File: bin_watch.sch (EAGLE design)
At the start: 69 parts, among them IC1 MEGA48/88/168-AU, Q1 8MHz, T1 NX3008NBKV, T2 NX3008NBKV, T3 NX3008NBKV, T4 NX3008NBKV, T5 PMDT670UPE, T6 PMDT670UPE, T7 PMDT670UPE

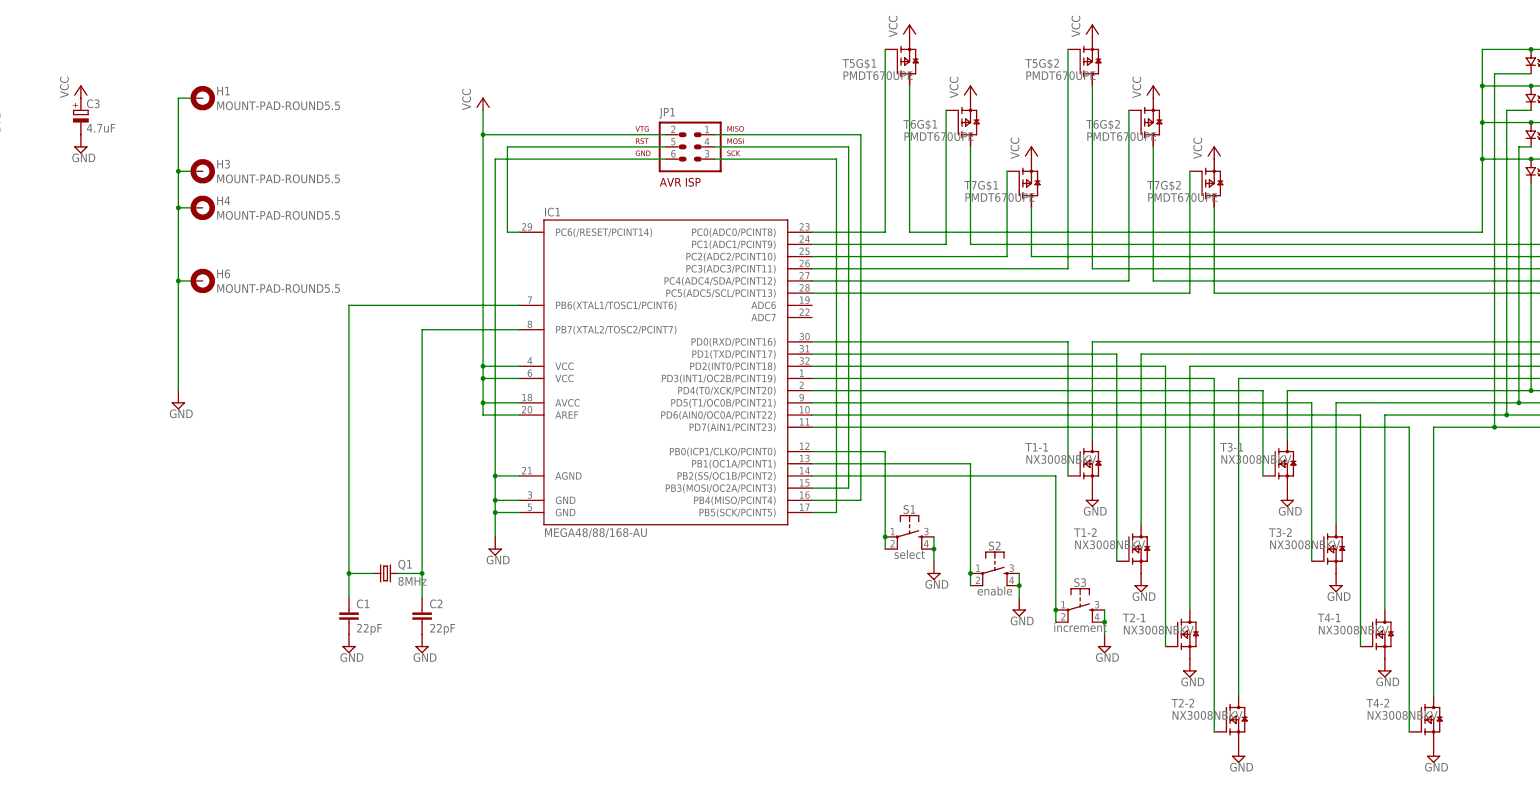
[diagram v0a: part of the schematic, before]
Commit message: Route cleanup
I ditched the auto-routed traces, and hand-routed everything. This should be much easier to work with.
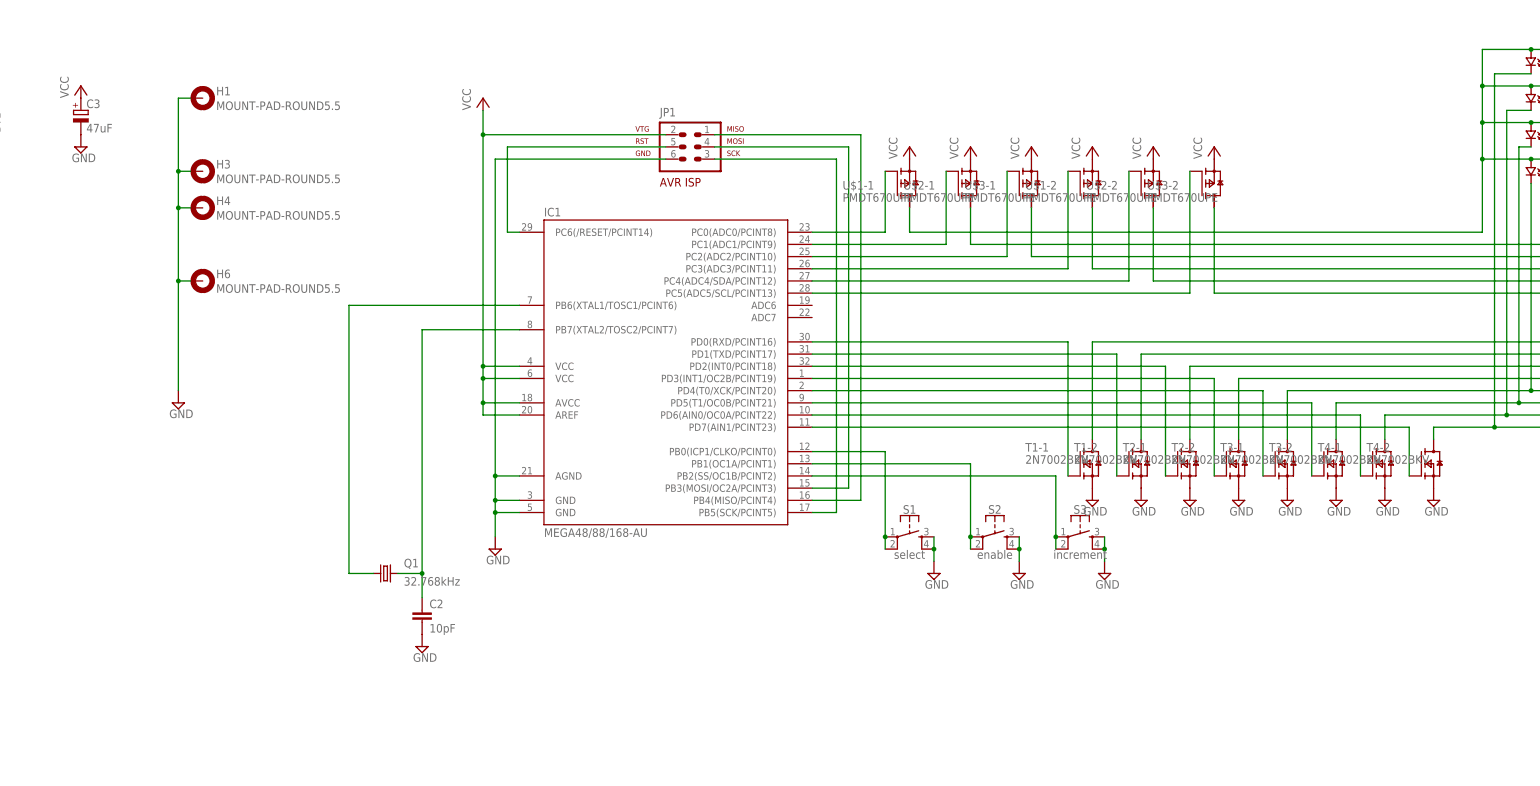
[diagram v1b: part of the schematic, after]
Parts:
- removed C1: 22pF, rcl:C-EUC0805
- removed T5, T6, T7: PMDT670UPE, nxp_60:PMDT670UPE
- added U$1, U$2, U$3: PMDT670UPE, nxp_60:PMDT670UPE
- C2: value 22pF -> 10pF
- C3: value 4.7uF -> 47uF
- Q1: value 8MHz -> 32.768kHz; device crystal:CRYSTALCTS406 -> crystal-geyer_V1_0:KX-327-NHF
- T1, T2, T3, T4: value NX3008NBKV -> 2N7002BKV
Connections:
- net XTAL2 renamed XTAL_N
- removed net XTAL1: C1.1, IC1.PB6(XTAL1/TOSC1/PCINT6), Q1.1
- new net XTAL_P: IC1.PB6(XTAL1/TOSC1/PCINT6), Q1.1
- net BLOCK: now also U$3-2.D; no longer T7G$2.D
- net BLOCK0: now also U$1-1.D; no longer T5G$1.D
- net BLOCK1: now also U$2-1.D; no longer T6G$1.D
- net BLOCK2: now also U$3-1.D; no longer T7G$1.D
- net BLOCK3: now also U$1-2.D; no longer T5G$2.D
- net BLOCK4: now also U$2-2.D; no longer T6G$2.D
- net GND: no longer C1.2
- net PC0: now also U$1-1.G; no longer T5G$1.G
- net PC1: now also U$2-1.G; no longer T6G$1.G
- net PC2: now also U$3-1.G; no longer T7G$1.G
- net PC3: now also U$1-2.G; no longer T5G$2.G
- net PC4: now also U$2-2.G; no longer T6G$2.G
- net PC5: now also U$3-2.G; no longer T7G$2.G
- net VCC: now also U$1-1.S, U$1-2.S, U$2-1.S, U$2-2.S, U$3-1.S, U$3-2.S; no longer T5G$1.S, T5G$2.S, T6G$1.S, T6G$2.S, T7G$1.S, T7G$2.S
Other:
- moved on the sheet: S2, S3, T1-2, T2-1, T2-2, T3-2, T4-1, T4-2

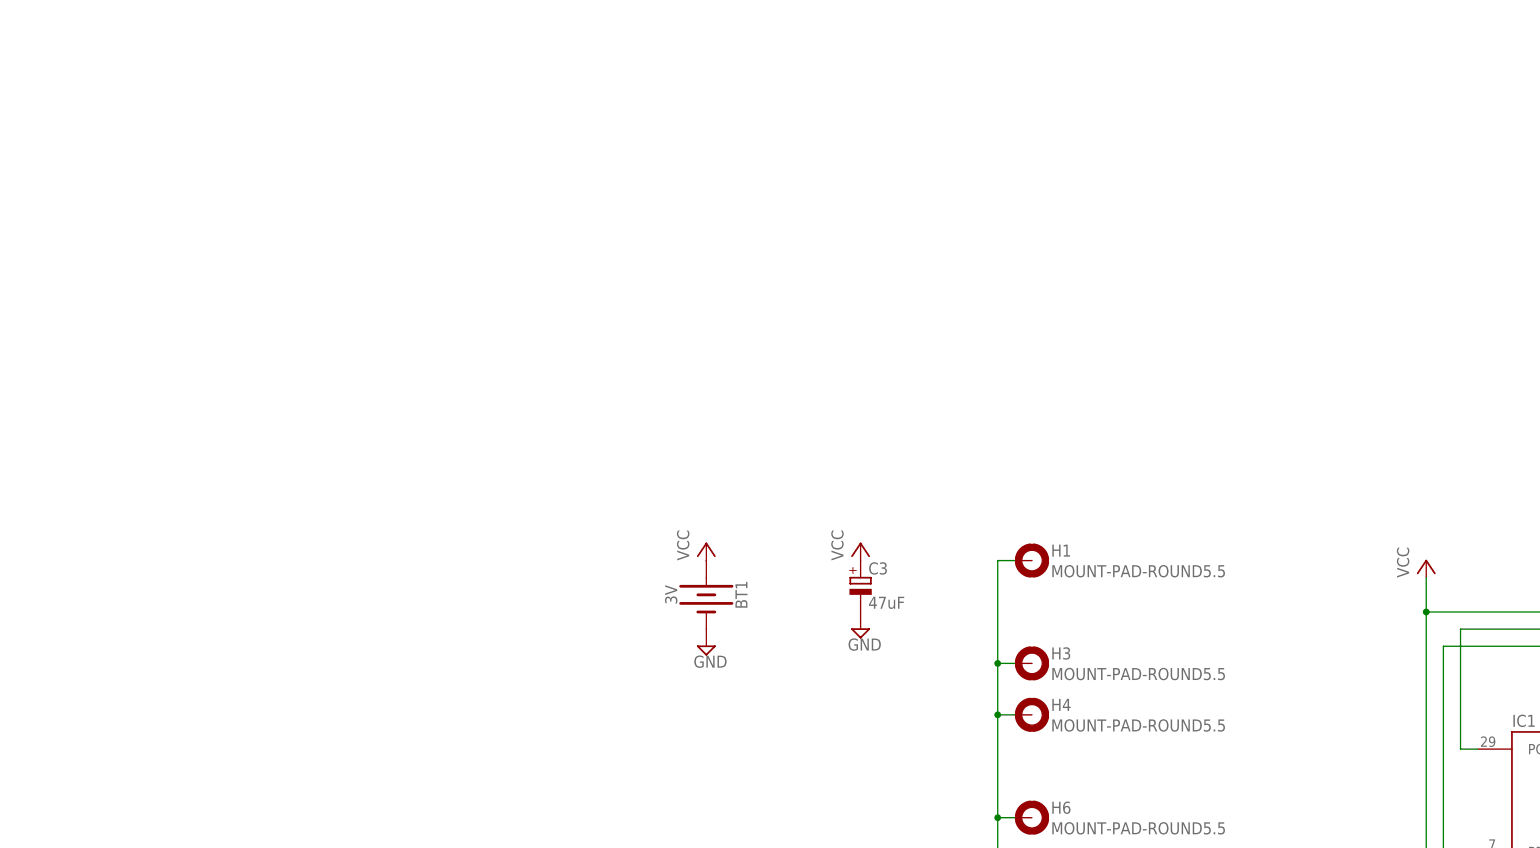
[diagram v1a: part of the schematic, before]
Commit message: Switched to Li-ion
The button cell i not up to the task, so we need a Li-ion battery.
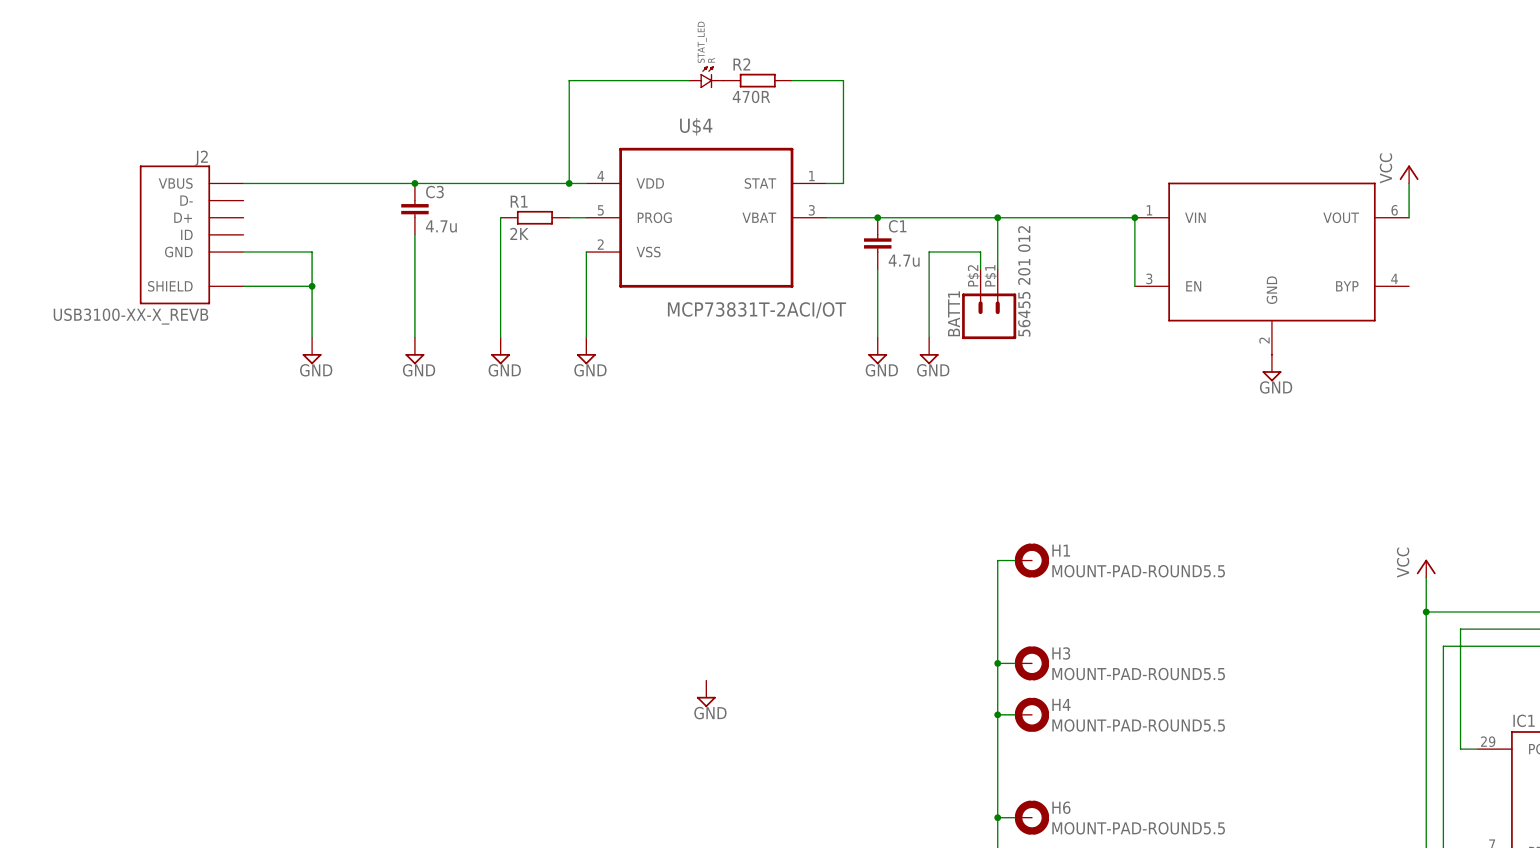
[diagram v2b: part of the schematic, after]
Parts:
- removed BT1: 3V, SparkFun-Batteries:BATTERY-12MM_SMD
- added BATT1: 56455 201 012, SparkFun-Connectors:CONN_02PTH2
- added C1: 4.7u, rcl:C-EUC0805
- added J2: USB3100-XX-X_REVB, USB3100-XX-X_REVB:USB3100-XX-X_REVB
- added R1: 2K, rcl:R-EU_R0805
- added R2: 470R, rcl:R-EU_R0805
- added STAT_LED: R, standardparts:LED.0603
- added U$4: MCP73831T-2ACI/OT, Microchip_By_element14_Batch_1:MCP73831T-2ACI/OT
- added U$5: MIC5319-3.3YD5-TR, pmg-library:MIC5319-3.3YD5-TR
- C3: value 47uF -> 4.7u; device rcl:CPOL-EU153CLV-0505 -> rcl:C-EUC0805
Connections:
- new net N$3: R2.1, STAT_LED.2
- new net PROG: R1.2, U$4.PROG
- new net STAT: R2.2, U$4.STAT
- new net VBATT: BATT1.1, C1.1, U$4.VBAT, U$5.EN, U$5.VIN
- new net VBUS: C3.1, J2.VBUS, STAT_LED.1, U$4.VDD
- net GND: now also BATT1.2, C1.2, C3.2, J2.GND, J2.SHIELD, R1.1, U$4.VSS, U$5.GND; no longer BT1.-, C3.-
- net VCC: now also U$5.VOUT; no longer BT1.+, C3.+

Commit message: Switched to switching supply
The linear regulator is not very efficient, swapping it for a buck converter.
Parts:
- removed J2: USB3100-XX-X_REVB, USB3100-XX-X_REVB:USB3100-XX-X_REVB
- removed U$2: PMDT670UPE, nxp_60:PMDT670UPE
- removed U$4: MCP73831T-2ACI/OT, Microchip_By_element14_Batch_1:MCP73831T-2ACI/OT
- removed U$5: MIC5319-3.3YD5-TR, pmg-library:MIC5319-3.3YD5-TR
- added C4: 3p, rcl:C-EUC0805
- added C5: (no value), rcl:CPOL-EUB/3528-21R
- added J1: USB3100-XX-X_REVB, USB3100-XX-X_REVB:USB3100-XX-X_REVB
- added L1: 2.2u, inductor:COIL-HI
- added R3: 294K, rcl:R-EU_R0805
- added R4: 470R, rcl:R-EU_R0805
- added T6: PMDT670UPE, nxp_60:PMDT670UPE
- added U1: MCP73831T-2ACI/OT, Microchip_By_element14_Batch_1:MCP73831T-2ACI/OT
- added U2: RT8059, pmg-library:RT8059
- C1: value 4.7u -> 10pF
- C2: value 10pF -> 4.7u
- R2: value 470R -> 1M33
- renumbered U$1 to T5, U$3 to T7
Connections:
- new net ADC6: IC1.ADC6
- new net ADC7: IC1.ADC7
- new net FB: C4.1, R2.1, R3.2, U2.FB
- new net LX: L1.L, U2.LX
- net BLOCK1: now also T6-1.D; no longer U$2-1.D
- net BLOCK4: now also T6-2.D; no longer U$2-2.D
- net GND: now also C5.-, J1.GND, J1.SHIELD, R3.1, U1.VSS, U2.GND; no longer J2.GND, J2.SHIELD, U$4.VSS, U$5.GND
- net N$3: now also R4.1; no longer R2.1
- net PC1: now also T6-1.G; no longer U$2-1.G
- net PC4: now also T6-2.G; no longer U$2-2.G
- net PROG: now also U1.PROG; no longer U$4.PROG
- net STAT: now also R4.2, U1.STAT; no longer R2.2, U$4.STAT
- net VBATT: now also C3.1, U1.VBAT, U2.EN, U2.VIN; no longer C1.1, U$4.VBAT, U$5.EN, U$5.VIN
- net VBUS: now also C2.1, J1.VBUS, U1.VDD; no longer C3.1, J2.VBUS, U$4.VDD
- net VCC: now also C4.2, C5.+, L1.R, R2.2, T6-1.S, T6-2.S; no longer U$2-1.S, U$2-2.S, U$5.VOUT
- net XTAL_N: now also C1.1; no longer C2.1
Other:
- moved on the sheet: BATT1, C1, C2, C3, H1, H3, H4, H6, R1, R2, S1, S2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

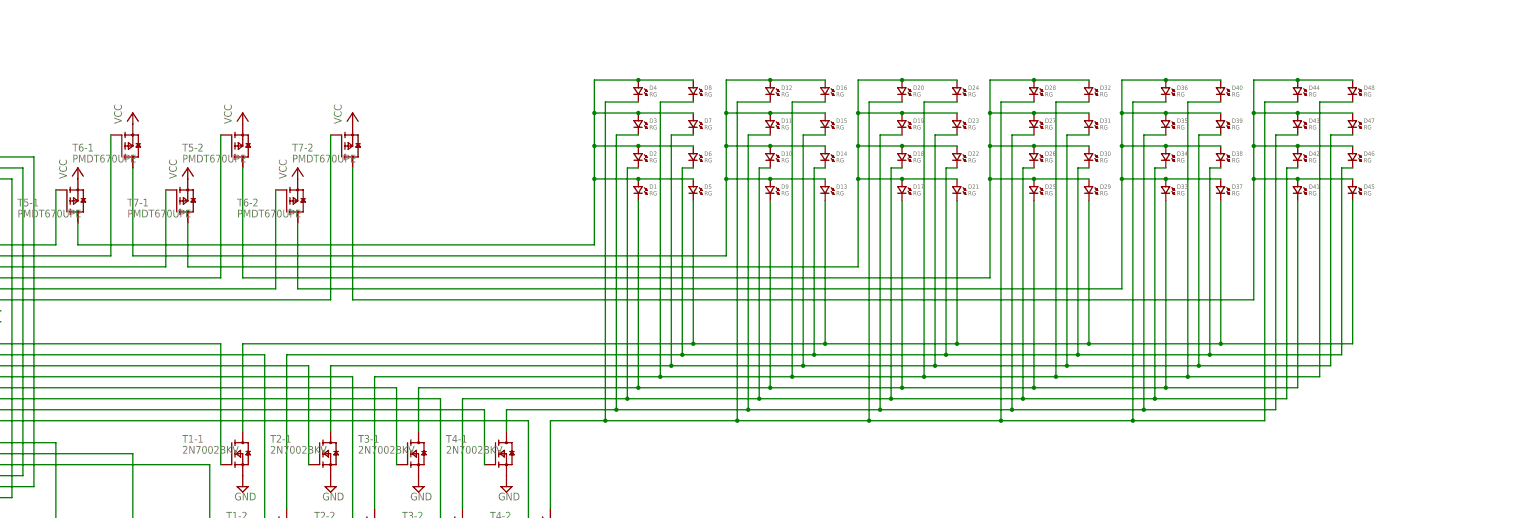
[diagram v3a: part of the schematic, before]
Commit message: Added I limiting resistors
Relying on the FETs to limit the current to diodes is not very safe, so added resistors to do that. It's a tight squeeze, but it fits.
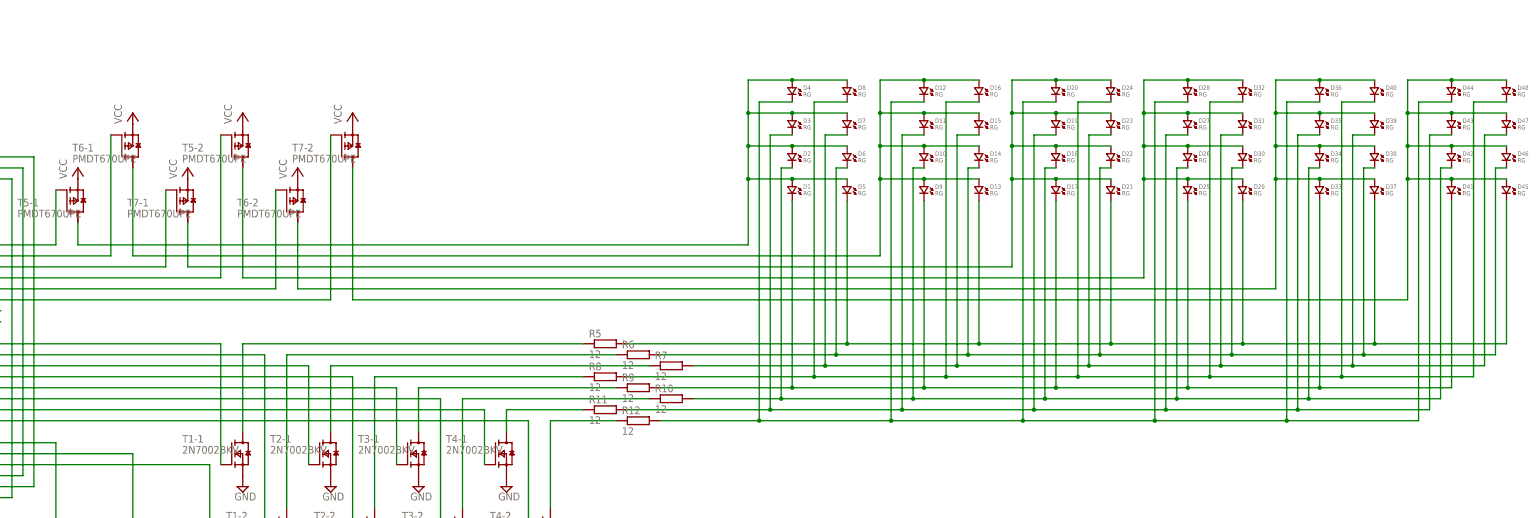
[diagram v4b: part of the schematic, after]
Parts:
- added R10, R11, R12, R5, R6, R7, R8, R9: 12, rcl:R-EU_R0603
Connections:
- new net N$1: R10.1, T3-2.D
- new net N$2: R11.1, T4-1.D
- new net N$4: R12.1, T4-2.D
- new net N$5: R9.1, T3-1.D
- new net N$6: R5.1, T1-1.D
- new net N$7: R6.1, T1-2.D
- new net N$8: R7.1, T2-1.D
- new net N$9: R8.1, T2-2.D
- net LIGHT0: now also R5.2; no longer T1-1.D
- net LIGHT1: now also R6.2; no longer T1-2.D
- net LIGHT2: now also R7.2; no longer T2-1.D
- net LIGHT3: now also R8.2; no longer T2-2.D
- net LIGHT4: now also R9.2; no longer T3-1.D
- net LIGHT5: now also R10.2; no longer T3-2.D
- net LIGHT6: now also R11.2; no longer T4-1.D
- net LIGHT7: now also R12.2; no longer T4-2.D
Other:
- moved on the sheet: D1, D10, D11, D12, D13, D14, D15, D16, D17, D18, D19, D2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
